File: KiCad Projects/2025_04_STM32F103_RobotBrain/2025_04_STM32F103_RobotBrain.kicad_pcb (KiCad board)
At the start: 2 copper layers, 90 x 80 mm, 47 parts, among them J1 USB_B_Mini, J10 CONN_TRACK, J11 CONN_UART, J2 CONN_MPU6050, J3 CONN_ULTRA, J4 CONN_SWD, J5 CONN_5V, J6 CONN_3V3, J7 CONN_DRIVE, J8 CONN_HAL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

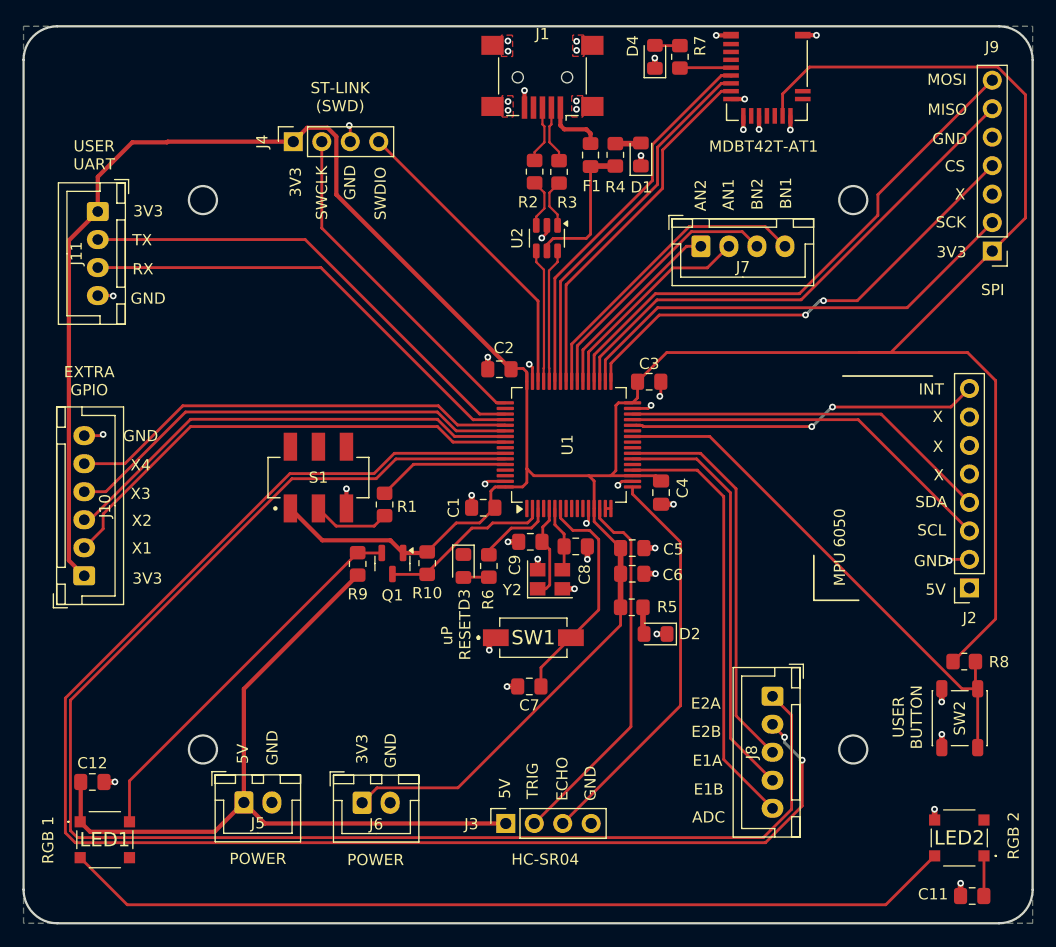
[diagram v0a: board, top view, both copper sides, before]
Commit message: Routing Complete
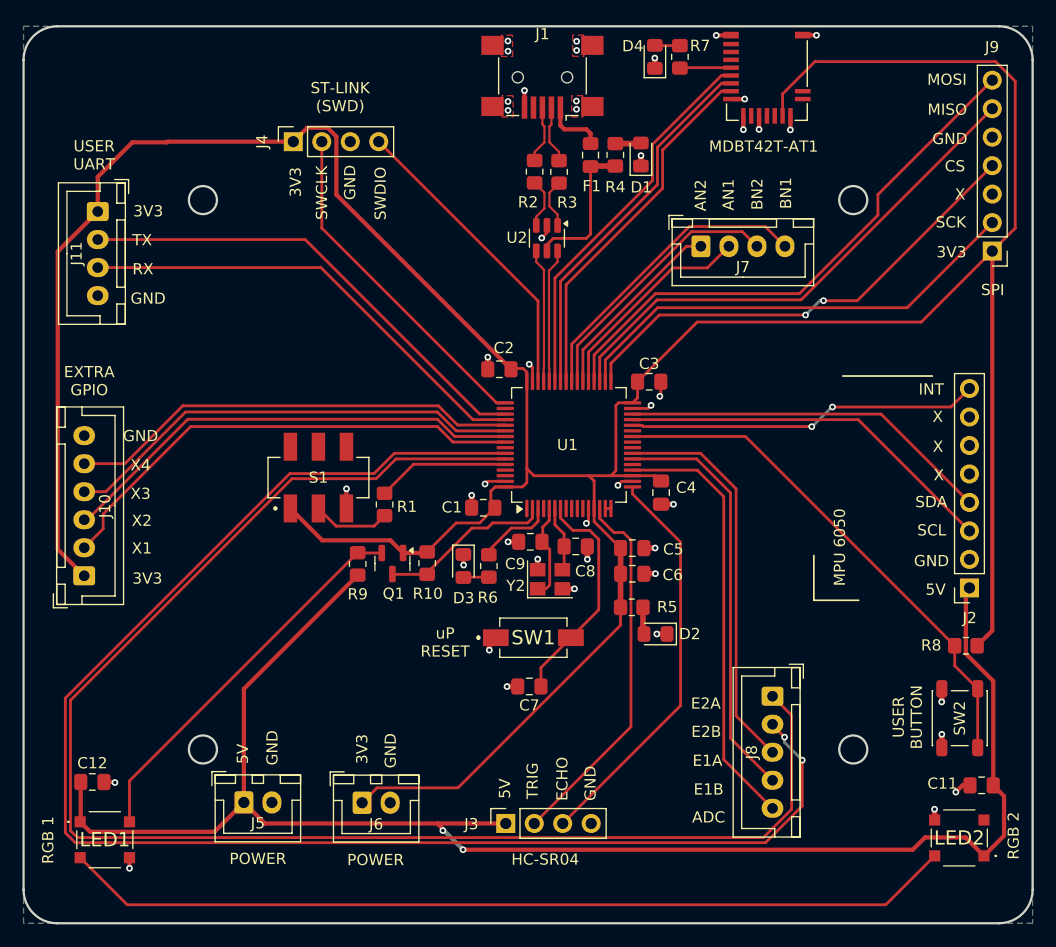
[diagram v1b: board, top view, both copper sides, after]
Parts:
- moved C11 9.91 mm to (177.6, 97.5)
- moved R8 1.42 mm to (176.2, 85.0), turned to 180 degrees
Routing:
- net +5V: track 71.8 -> 145.4 mm, vias 0 -> 2
- net GND: track 48.0 -> 43.8 mm, vias 46 -> 44
- net +3V3: track 309.7 -> 306.3 mm
- net /uBUTTON: track 47.9 -> 46.4 mm

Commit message: PCB Complete (with Gerber)
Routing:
- net /E2B: track 136.7 -> 140.4 mm
- net /IMU_I2C_SCL: track 34.2 -> 37.7 mm
- net /E1A: track 35.4 -> 37.0 mm
- net /BN1: track 27.4 -> 29.0 mm
- net +5V: track 145.4 -> 146.7 mm
- net Net-(LED1-DOUT): track 79.8 -> 78.5 mm
- net /E2A: track 135.7 -> 136.9 mm
- net /BN2: track 23.9 -> 24.9 mm
- net /IMU_I2C_SDA: track 33.3 -> 34.3 mm
- net /PS2_CS: track 42.9 -> 42.0 mm
- net /X4: track 40.4 -> 41.2 mm
- net /BL_WAKEUP: track 34.4 -> 35.1 mm
- net /PS2_SCK: track 41.5 -> 40.9 mm
- net /PS2_MOSI: track 49.1 -> 48.5 mm
- net /IMU_INT: track 31.2 -> 31.7 mm
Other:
- board text added: "uP BOOT"
